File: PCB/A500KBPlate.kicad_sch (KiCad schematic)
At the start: 116 parts

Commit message: shifted A500KB connectors down on the PCB by 9mm This change allows angled connectors in conjunction with Dupont plugs for connection to the A500 mainboard.
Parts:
- H3, H4: footprint MountingHole:MountingHole_4.3mm_M4 -> MountingHole:MountingHole_4mm
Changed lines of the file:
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@@
 			)
 		)
-		(property "Footprint" "MountingHole:MountingHole_4.3mm_M4"
+		(property "Footprint" "MountingHole:MountingHole_4mm"
 			(at 57.15 238.125 0)
 			(effects
@@
 			)
 		)
-		(property "Footprint" "MountingHole:MountingHole_4.3mm_M4"
+		(property "Footprint" "MountingHole:MountingHole_4mm"
 			(at 75.565 238.125 0)
 			(effects

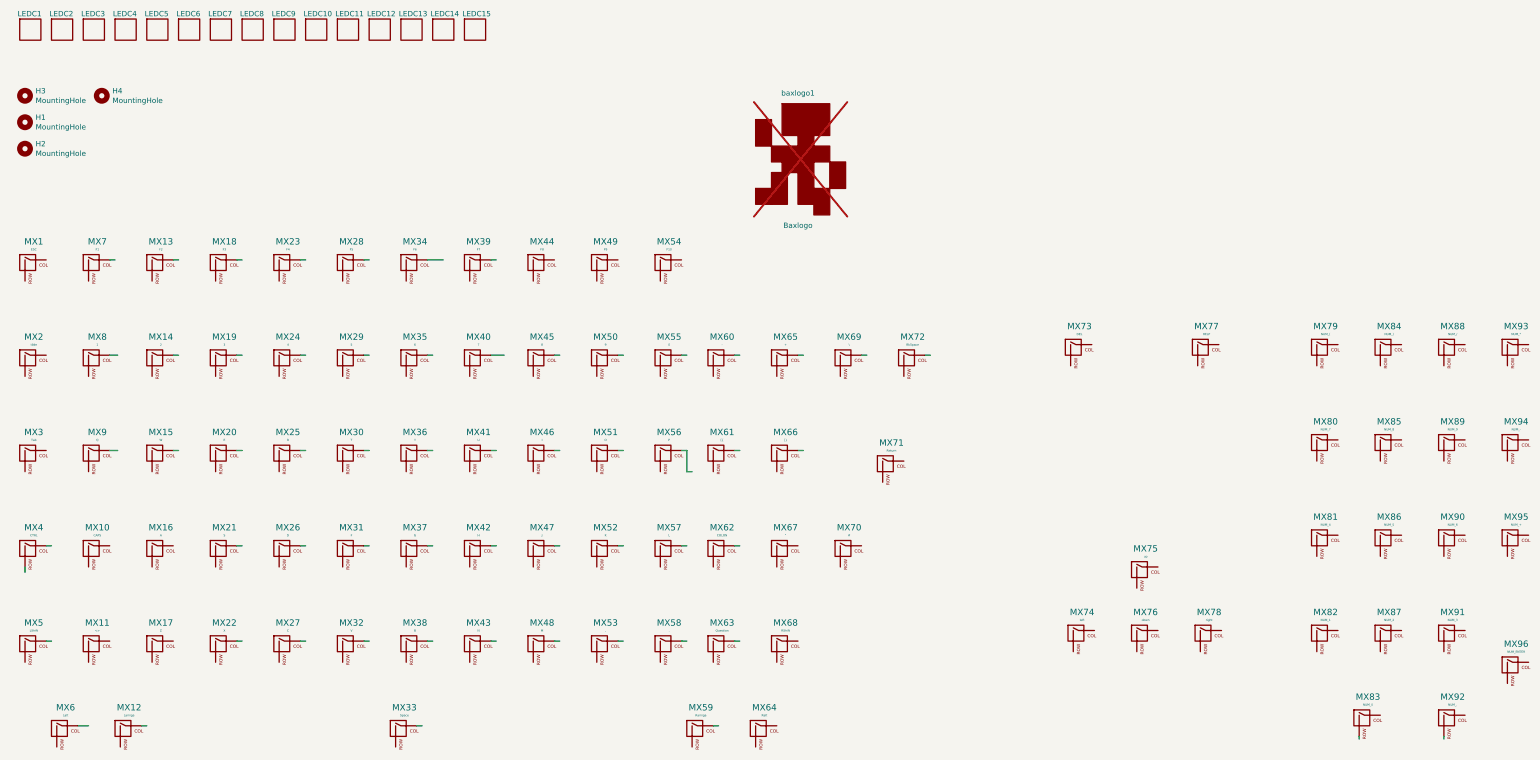
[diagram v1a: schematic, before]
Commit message: added US-Only version (large Return, 2.75U LShift)
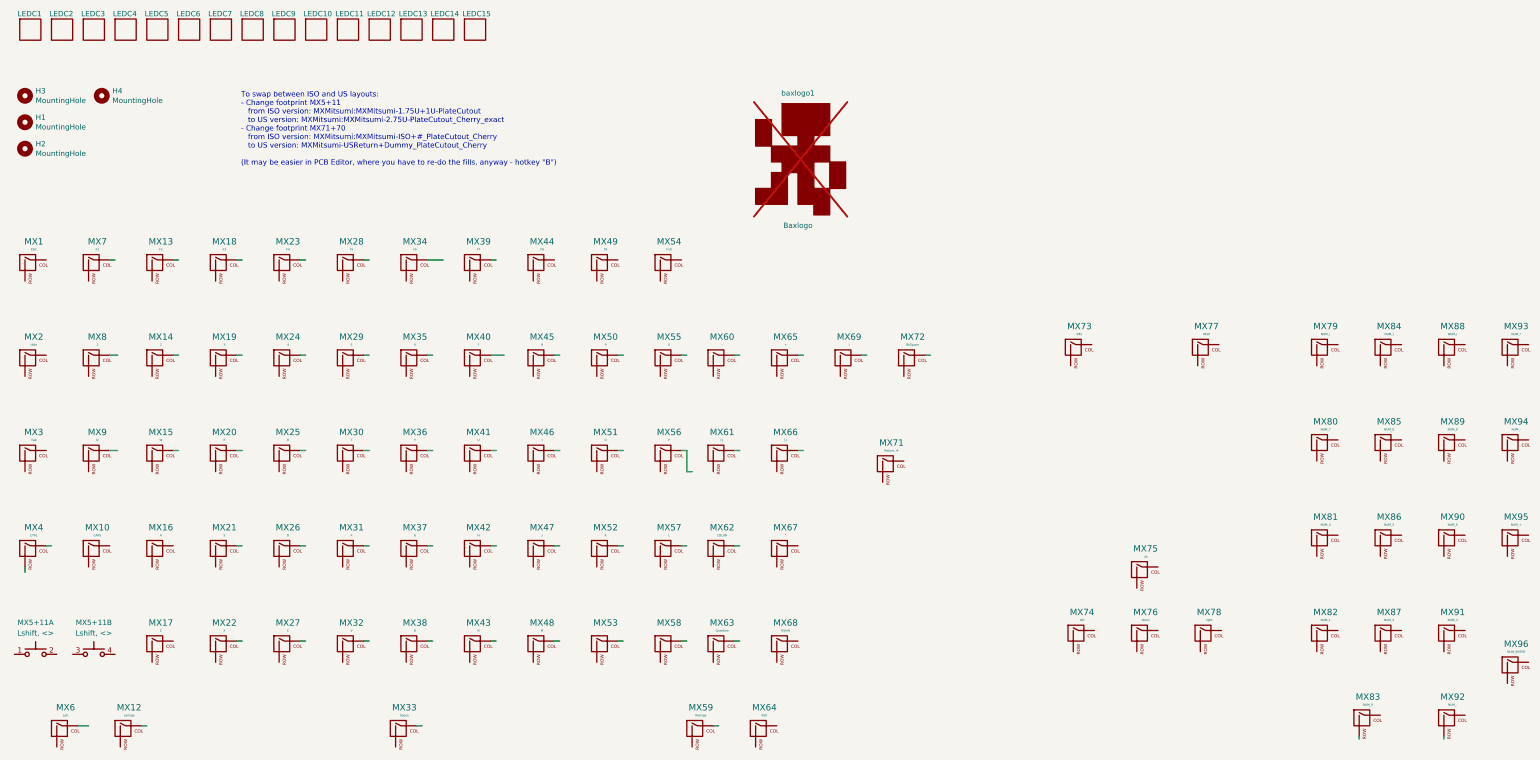
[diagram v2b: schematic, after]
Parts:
- removed MX11: <>, MXMitsumi:MXMitsumi-1U-PlateCutout_Square, symbol MX_Hybrid:MX-NoLED
- removed MX5: LShift, MXMitsumi:MXMitsumi-1.75U-PlateCutout, symbol MX_Hybrid:MX-NoLED
- removed MX70: #, MXMitsumi:MXMitsumi-1U-PlateCutout_Square, symbol MX_Hybrid:MX-NoLED
- added MX5+11: Lshift, <>, MXMitsumi:MXMitsumi-2.75U-PlateCutout_Cherry_exact, symbol Switch:SW_Push_Dual_x2
- MX71: value Return -> Return, #; footprint MXMitsumi:MXMitsumi-ISO-PlateCutout_Cherry -> MXMitsumi:MXMitsumi-ISO+#_PlateCutout_Cherry
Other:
- note added: "To swap between ISO and US layouts: - Change footprint MX5+11 from ISO version: MXMitsumi:MXMitsumi-1.75U+1U-PlateCutout to US version: MXMitsumi:MXMitsumi-2.75U-PlateCutout_Cherry_exact - Change footprint MX71+70 from ISO version: MXMitsumi:MXMitsumi-ISO+#_PlateCutout_Cherry to US version: MXMitsumi-USReturn+Dummy_PlateCutout_Cherry (It may be easier in PCB Editor, where you have to re-do the fi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"
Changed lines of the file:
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@@
 	(wire
 		(pts
-			(xy 62.23 368.935) (xy 63.5 368.935)
-		)
-		(stroke
-			(width 0)
-			(type default)
-		)
-	)
-	(wire
-		(pts
 			(xy 139.7 368.935) (xy 138.43 368.935)
 		)
@@
 		)
 	)
+	(text "To swap between ISO and US layouts:\n- Change footprint MX5+11 \n   from ISO version: MXMitsumi:MXMitsumi-1.75U+1U-PlateCutout\n   to US version: MXMitsumi:MXMitsumi-2.75U-PlateCutout_Cherry_exact\n- Change footprint MX71+70\n   from ISO version: MXMitsumi:MXMitsumi-ISO+#_PlateCutout_Cherry\n   to US version: MXMitsumi-USReturn+Dummy_PlateCutout_Cherry\n\n(It may be easier in PCB Editor, where you have to re-do the fills, anyway - hotkey \"B\")"
+		(exclude_from_sim no)
+		(at 108.966 246.126 0)
+		(effects
+			(font
+				(size 1.27 1.27)
+			)
+			(justify left)
+		)
+	)
 	(symbol
 		(lib_id "MX_Hybrid:MX-NoLED")
@@
 	(symbol
 		(lib_id "MX_Hybrid:MX-NoLED")
-		(at 254 347.345 0)
-		(unit 1)
-		(exclude_from_sim no)
-		(in_bom yes)
-		(on_board yes)
-		(dnp no)
-		(property "Reference" "MX70"
-			(at 254.8382 341.6808 0)
-			(effects
-				(font
-					(size 1.524 1.524)
-				)
-			)
-		)
-		(property "Value" "#"
-			(at 254.8382 343.5604 0)
-			(effects
-				(font
-					(size 0.508 0.508)
-				)
-			)
-		)
-		(property "Footprint" "MXMitsumi:MXMitsumi-1U-PlateCutout_Square"
-			(at 238.125 347.98 0)
-			(effects
-				(font
-					(size 1.524 1.524)
-				)
-				(hide yes)
-			)
-		)
-		(property "Datasheet" ""
-			(at 238.125 347.98 0)
-			(effects
-				(font
-					(size 1.524 1.524)
-				)
-				(hide yes)
-			)
-		)
-		(property "Description" ""
-			(at 254 347.345 0)
-			(effects
-				(font
-					(size 1.27 1.27)
-				)
-				(hide yes)
-			)
-		)
-		(pin "2"
-		)
-		(pin "1"
-		)
-		(instances
-			(project ""
-				(path "/14d2be24-e894-4dc3-9020-12862a44e771"
-					(reference "MX70")
-					(unit 1)
-				)
-			)
-		)
-	)
-	(symbol
-		(lib_id "MX_Hybrid:MX-NoLED")
-		(at 58.42 370.205 0)
-		(unit 1)
-		(exclude_from_sim no)
-		(in_bom yes)
-		(on_board yes)
-		(dnp no)
-		(property "Reference" "MX5"
-			(at 59.2582 364.5408 0)
-			(effects
-				(font
-					(size 1.524 1.524)
-				)
-			)
-		)
-		(property "Value" "LShift"
-			(at 59.2582 366.4204 0)
-			(effects
-				(font
-					(size 0.508 0.508)
-				)
-			)
-		)
-		(property "Footprint" "MXMitsumi:MXMitsumi-1.75U-PlateCutout"
-			(at 42.545 370.84 0)
-			(effects
-				(font
-					(size 1.524 1.524)
-				)
-				(hide yes)
-			)
-		)
-		(property "Datasheet" ""
-			(at 42.545 370.84 0)
-			(effects
-				(font
-					(size 1.524 1.524)
-				)
-				(hide yes)
-			)
-		)
-		(property "Description" ""
-			(at 58.42 370.205 0)
-			(effects
-				(font
-					(size 1.27 1.27)
-				)
-				(hide yes)
-			)
-		)
-		(pin "1"
-		)
-		(pin "2"
-		)
-		(instances
-			(project ""
-				(path "/14d2be24-e894-4dc3-9020-12862a44e771"
-					(reference "MX5")
-					(unit 1)
-				)
-			)
-		)
-	)
-	(symbol
-		(lib_id "MX_Hybrid:MX-NoLED")
-		(at 73.66 370.205 0)
-		(unit 1)
-		(exclude_from_sim no)
-		(in_bom yes)
-		(on_board yes)
-		(dnp no)
-		(property "Reference" "MX11"
-			(at 74.4982 364.5408 0)
-			(effects
-				(font
-					(size 1.524 1.524)
-				)
-			)
-		)
-		(property "Value" "<>"
-			(at 74.4982 366.4204 0)
-			(effects
-				(font
-					(size 0.508 0.508)
-				)
-			)
-		)
-		(property "Footprint" "MXMitsumi:MXMitsumi-1U-PlateCutout_Square"
-			(at 57.785 370.84 0)
-			(effects
-				(font
-					(size 1.524 1.524)
-				)
-				(hide yes)
-			)
-		)
-		(property "Datasheet" ""
-			(at 57.785 370.84 0)
-			(effects
-				(font
-					(size 1.524 1.524)
-				)
-				(hide yes)
-			)
-		)
-		(property "Description" ""
-			(at 73.66 370.205 0)
-			(effects
-				(font
-					(size 1.27 1.27)
-				)
-				(hide yes)
-			)
-		)
-		(pin "1"
-		)
-		(pin "2"
-		)
-		(instances
-			(project ""
-				(path "/14d2be24-e894-4dc3-9020-12862a44e771"
-					(reference "MX11")
-					(unit 1)
-				)
-			)
-		)
-	)
-	(symbol
-		(lib_id "MX_Hybrid:MX-NoLED")
 		(at 88.9 370.205 0)
 		(unit 1)
@@
 			)
 		)
-		(property "Value" "Return"
+		(property "Value" "Return, #"
 			(at 264.9982 323.2404 0)
 			(effects
@@
 			)
 		)
-		(property "Footprint" "MXMitsumi:MXMitsumi-ISO-PlateCutout_Cherry"
+		(property "Footprint" "MXMitsumi:MXMitsumi-ISO+#_PlateCutout_Cherry"
 			(at 248.285 327.66 0)
 			(effects
@@
 	)
 	(symbol
+		(lib_id "Switch:SW_Push_Dual_x2")
+		(at 59.69 372.11 0)
+		(unit 1)
+		(exclude_from_sim no)
+		(in_bom yes)
+		(on_board yes)
+		(dnp no)
+		(fields_autoplaced yes)
+		(property "Reference" "MX5+11"
+			(at 59.69 364.49 0)
+			(effects
+				(font
+					(size 1.27 1.27)
+				)
+			)
+		)
+		(property "Value" "Lshift, <>"
+			(at 59.69 367.03 0)
+			(effects
+				(font
+					(size 1.27 1.27)
+				)
+			)
+		)
+		(property "Footprint" "MXMitsumi:MXMitsumi-2.75U-PlateCutout_Cherry_exact"
+			(at 59.69 367.03 0)
+			(effects
+				(font
+					(size 1.27 1.27)
+				)
+				(hide yes)
+			)
+		)
+		(property "Datasheet" "~"
+			(at 59.69 367.03 0)
+			(effects
+				(font
+					(size 1.27 1.27)
+				)
+				(hide yes)
+			)
+		)
+		(property "Description" "Push button switch, generic, separate symbols, four pins"
+			(at 59.69 372.11 0)
+			(effects
+				(font
+					(size 1.27 1.27)
+				)
+				(hide yes)
+			)
+		)
+		(pin "1"
+		)
+		(pin "3"
+		)
+		(pin "4"
+		)
+		(pin "2"
+		)
+		(instances
+			(project ""
+				(path "/14d2be24-e894-4dc3-9020-12862a44e771"
+					(reference "MX5+11")
+					(unit 1)
+				)
+			)
+		)
+	)
+	(symbol
 		(lib_id "LED_Cutout_LIB:LED_Cutout")
 		(at 88.9 222.25 0)
@@
 				)
 			)
+		)
+	)
+	(symbol
+		(lib_id "Switch:SW_Push_Dual_x2")
+		(at 73.66 372.11 0)
+		(unit 2)
+		(exclude_from_sim no)
+		(in_bom yes)
+		(on_board yes)
+		(dnp no)
+		(property "Reference" "MX5+11"
+			(at 73.66 364.49 0)
+			(effects
+				(font
+					(size 1.27 1.27)
+				)
+			)
+		)
+		(property "Value" "Lshift, <>"
+			(at 73.66 367.03 0)
+			(effects
+				(font
+					(size 1.27 1.27)
+				)
+			)
+		)
+		(property "Footprint" "MXMitsumi:MXMitsumi-2.75U-PlateCutout_Cherry_exact"
+			(at 73.66 367.03 0)
+			(effects
+				(font
+					(size 1.27 1.27)
+				)
+				(hide yes)
+			)
+		)
+		(property "Datasheet" "~"
+			(at 73.66 367.03 0)
+			(effects
+				(font
+					(size 1.27 1.27)
+				)
+				(hide yes)
+			)
+		)
+		(property "Description" "Push button switch, generic, separate symbols, four pins"
+			(at 73.66 372.11 0)
+			(effects
+				(font
+					(size 1.27 1.27)
+				)
+				(hide yes)
+			)
+		)
+		(pin "1"
+		)
+		(pin "3"
+		)
+		(pin "4"
+		)
+		(pin "2"
+		)
+		(instances
+			(project ""
+				(path "/14d2be24-e894-4dc3-9020-12862a44e771"
+					(reference "MX5+11")
+					(unit 2)
+				)
+			)

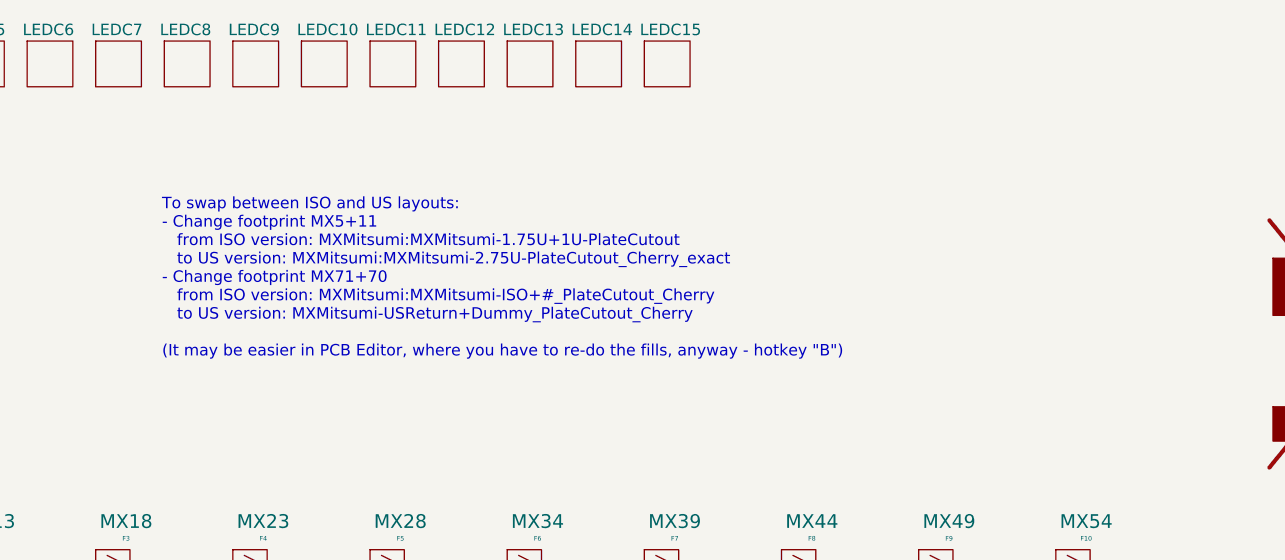
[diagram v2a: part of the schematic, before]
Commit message: corrected LShift on US version plate gerbers
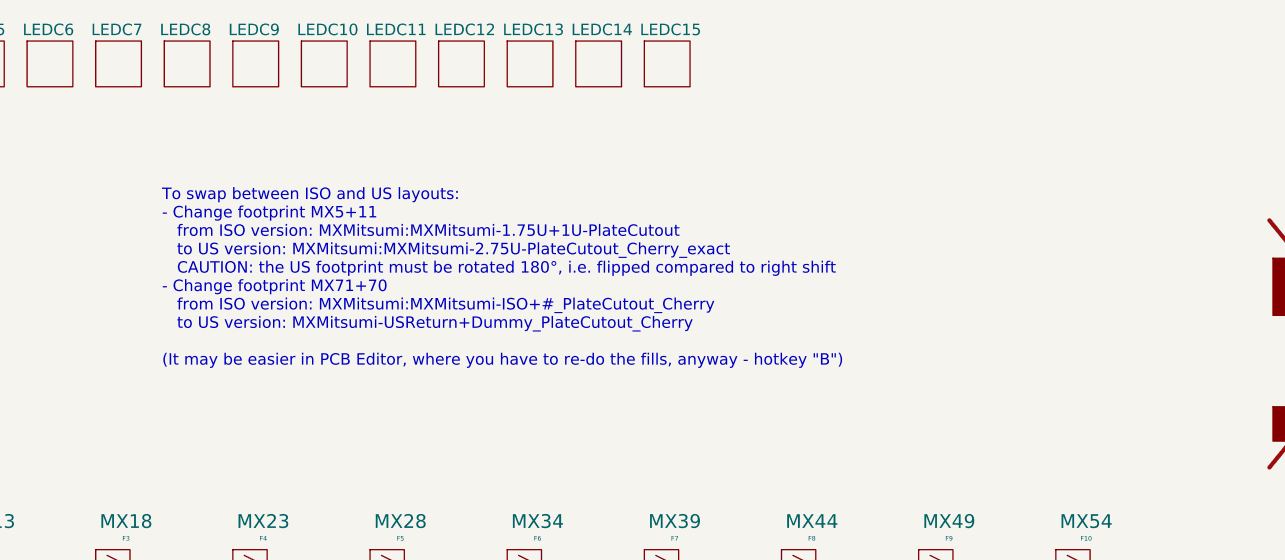
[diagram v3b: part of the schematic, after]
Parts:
- MX71: footprint MXMitsumi:MXMitsumi-ISO+#_PlateCutout_Cherry -> MXMitsumi:MXMitsumi-USReturn+Dummy_PlateCutout_Cherry
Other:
- note added: "To swap between ISO and US layouts: - Change footprint MX5+11 from ISO version: MXMitsumi:MXMitsumi-1.75U+1U-PlateCutout to US version: MXMitsumi:MXMitsumi-2.75U-PlateCutout_Cherry_exact CAUTION: the US footprint must be rotated 180°, i.e. flipped compared to right shift - Change footprint MX71+70 from ISO version: MXMitsumi:MXMitsumi-ISO+#_PlateCutout_Cherry to US version: MXMitsumi-USReturn+Dum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"
- note removed: "To swap between ISO and US layouts: - Change footprint MX5+11 from ISO version: MXMitsumi:MXMitsumi-1.75U+1U-PlateCutout to US version: MXMitsumi:MXMitsumi-2.75U-PlateCutout_Cherry_exact - Change footprint MX71+70 from ISO version: MXMitsumi:MXMitsumi-ISO+#_PlateCutout_Cherry to US version: MXMitsumi-USReturn+Dummy_PlateCutout_Cherry (It may be easier in PCB Editor, where you have to re-do the fi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"
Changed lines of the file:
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@@
 (kicad_sch
-	(version 20231120)
+	(version 20250114)
 	(generator "eeschema")
-	(generator_version "8.0")
+	(generator_version "9.0")
 	(paper "A2")
 	(title_block
@@
 		(company "Henryk Richter")
 	)
+	(text "To swap between ISO and US layouts:\n- Change footprint MX5+11 \n   from ISO version: MXMitsumi:MXMitsumi-1.75U+1U-PlateCutout\n   to US version: MXMitsumi:MXMitsumi-2.75U-PlateCutout_Cherry_exact\n   CAUTION: the US footprint must be rotated 180°, i.e. flipped compared to right shift\n- Change footprint MX71+70\n   from ISO version: MXMitsumi:MXMitsumi-ISO+#_PlateCutout_Cherry\n   to US version: MXMitsumi-USReturn+Dummy_PlateCutout_Cherry\n\n(It may be easier in PCB Editor, where you have to re-do the fills, anyway - hotkey \"B\")"
+		(exclude_from_sim no)
+		(at 108.966 246.126 0)
+		(effects
+			(font
+				(size 1.27 1.27)
+			)
+			(justify left)
+		)
+	)
 	(wire
 		(pts
@@
 		)
 	)
-	(text "To swap between ISO and US layouts:\n- Change footprint MX5+11 \n   from ISO version: MXMitsumi:MXMitsumi-1.75U+1U-PlateCutout\n   to US version: MXMitsumi:MXMitsumi-2.75U-PlateCutout_Cherry_exact\n- Change footprint MX71+70\n   from ISO version: MXMitsumi:MXMitsumi-ISO+#_PlateCutout_Cherry\n   to US version: MXMitsumi-USReturn+Dummy_PlateCutout_Cherry\n\n(It may be easier in PCB Editor, where you have to re-do the fills, anyway - hotkey \"B\")"
-		(exclude_from_sim no)
-		(at 108.966 246.126 0)
-		(effects
-			(font
-				(size 1.27 1.27)
-			)
-			(justify left)
-		)
-	)
 	(symbol
 		(lib_id "MX_Hybrid:MX-NoLED")
@@
 			)
 		)
-		(property "Footprint" "MXMitsumi:MXMitsumi-ISO+#_PlateCutout_Cherry"
+		(property "Footprint" "MXMitsumi:MXMitsumi-USReturn+Dummy_PlateCutout_Cherry"
 			(at 248.285 327.66 0)
 			(effects
@@
 		)
 	)
+	(embedded_fonts no)
 )
